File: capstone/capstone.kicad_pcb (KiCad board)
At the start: 2 copper layers, 137.8 x 125.7 mm, 16 parts, among them J1 Conn_01x02, M1 Motor_Servo, M2 Motor_Servo, M3 Stepper_Motor_bipolar, M4 Stepper_Motor_bipolar, SW1 SW_Push, U1 PicoW

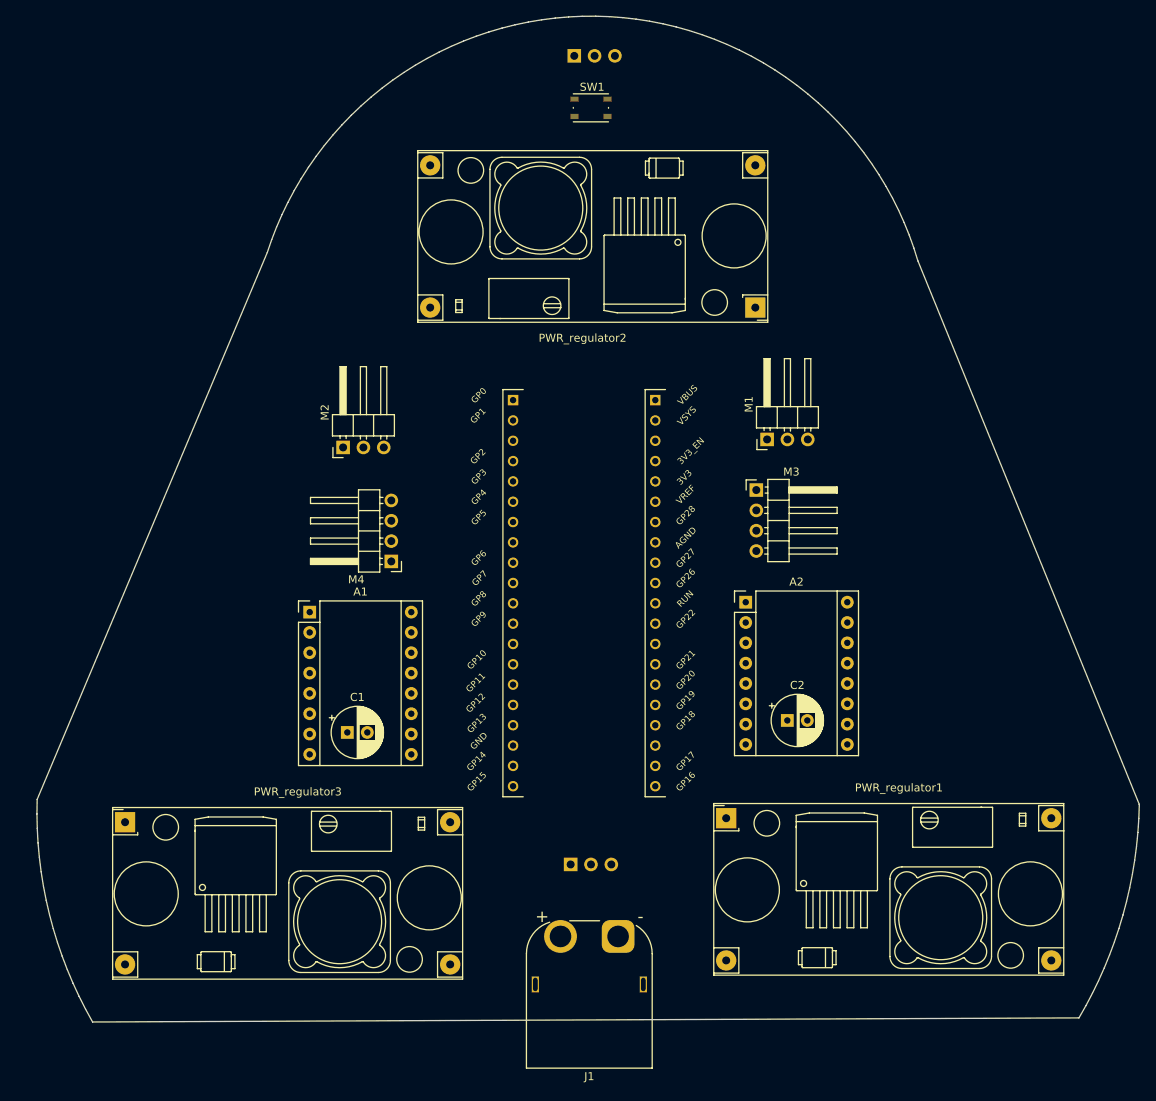
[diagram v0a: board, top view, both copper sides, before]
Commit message: remove 12v regulators + pcb traces
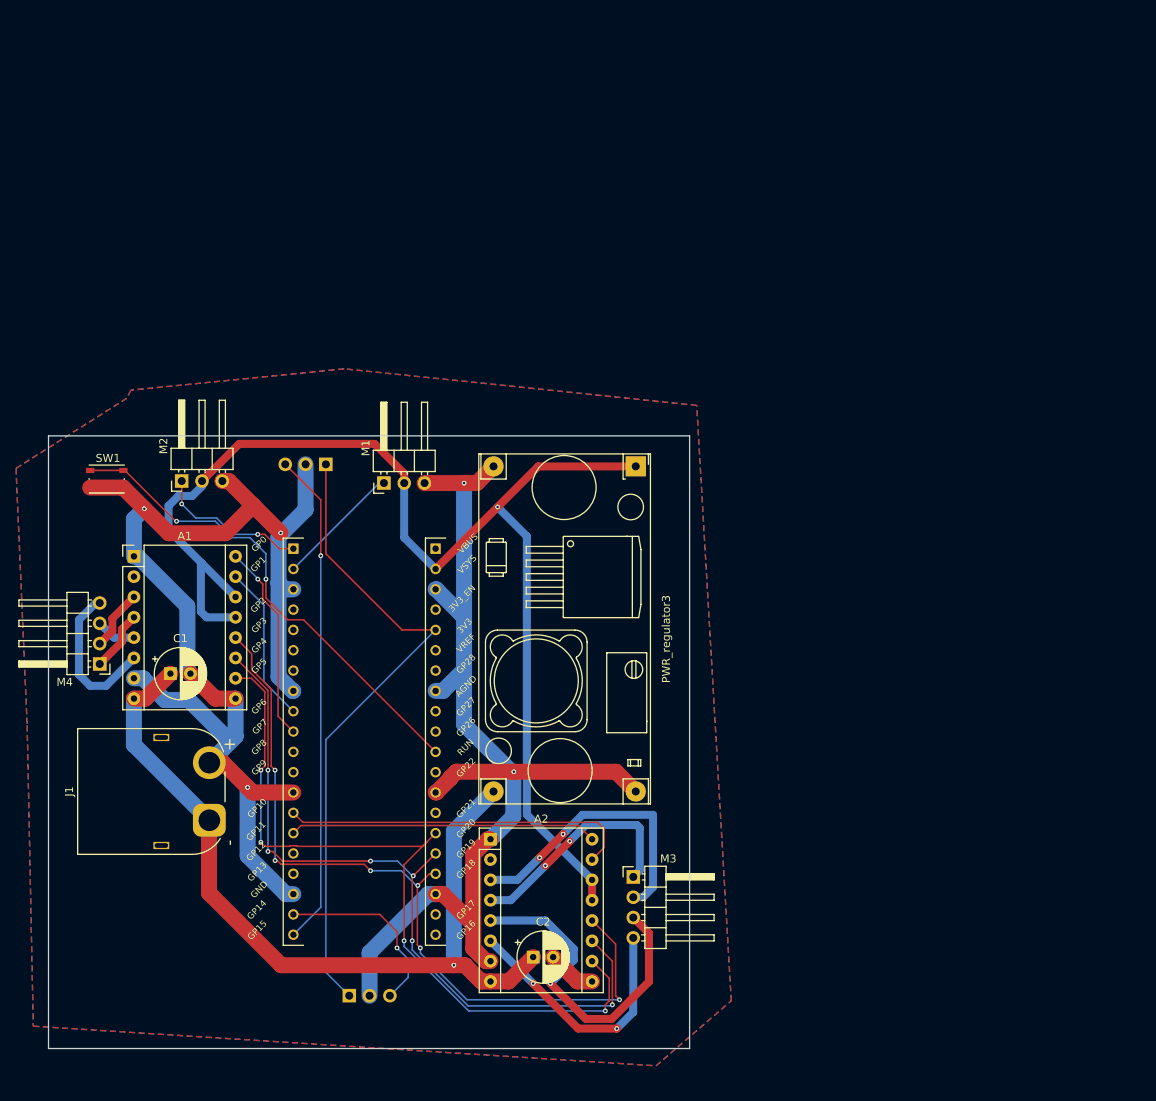
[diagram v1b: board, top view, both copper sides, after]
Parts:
- removed PWR_regulator1, PWR_regulator2: ~, capstone:YAAJ_DCDC_StepDown_LM2596
- moved PWR_regulator3 77.8 mm to (130.6, 88.5), turned to -90 degrees
- moved SW1 76.3 mm to (64.4, 90.1)
- moved IR_sensor2 59.8 mm to (91.8, 88.3), turned to 90 degrees
- moved J1 53.1 mm to (77.3, 132.8), turned to 90 degrees
- moved M3 50.7 mm to (130.2, 139.8)
- moved M1 48.2 mm to (99.1, 90.6)
- moved A2 43.5 mm to (112.4, 135.1)
- moved C2 43.4 mm to (117.7, 149.9)
- moved M4 38.6 mm to (63.6, 113.2)
- moved U1 33.1 mm to (96.5, 120.5)
- moved IR_sensor1 32.2 mm to (94.7, 154.7)
- moved C1 23.3 mm to (72.4, 114.4)
- moved A1 23.1 mm to (67.8, 99.8)
- moved M2 20.6 mm to (73.8, 90.4)
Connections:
- A1 pad 8: Stepper_PWR_12V -> 14V
- A2 pad 8: Stepper_PWR_12V -> 14V
- C1 pad 1: Stepper_PWR_12V -> 14V
- C2 pad 1: Stepper_PWR_12V -> 14V
- J1 pad 1: Lipo -> 14V
- M1 pad 2: /Servo_PWR_5V -> /PICO_PWR_5V
- M2 pad 2: /Servo_PWR_5V -> /PICO_PWR_5V
- PWR_regulator3 pad 3: Lipo -> 14V
- U1 pad 40: VBUS -> unconnected-(U1-VBUS-Pad40)
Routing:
- net GND: track 0.00 -> 292.1 mm, vias 0 -> 5
- net /PICO_PWR_5V: track 0.00 -> 158.1 mm, vias 0 -> 1
- net 14V: track 0.00 -> 104.2 mm, vias 0 -> 1
- net /mode_bit_3: track 0.00 -> 99.2 mm, vias 0 -> 6
- net /mode_bit_1: track 0.00 -> 96.4 mm, vias 0 -> 4
- net /mode_bit_2: track 0.00 -> 95.5 mm, vias 0 -> 6
- net +3V3: track 0.00 -> 81.4 mm
- net /GPIO15: track 0.00 -> 62.1 mm, vias 0 -> 1
- net /RUN: track 0.00 -> 61.1 mm, vias 0 -> 2
- net /GPIO10: track 0.00 -> 44.1 mm
- net /B1_2: track 0.00 -> 42.3 mm, vias 0 -> 1
- net /GPIO11: track 0.00 -> 38.4 mm
- net /A2_2: track 0.00 -> 35.7 mm, vias 0 -> 2
- net /B2_2: track 0.00 -> 32.5 mm, vias 0 -> 2
- net /A1_2: track 0.00 -> 29.2 mm, vias 0 -> 2
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- added copper zone on B.Cu, net GND
- added copper zone on F.Cu, net GND
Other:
- board size 137.8 x 125.7 mm -> 80.1 x 76.6 mm

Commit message: final pcb
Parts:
- added G***: LOGO, LOGO, F.Cu at (62.1, 142.5)
- moved IR_sensor1 2.82 mm to (94.4, 157.5)
- moved SW1 2.76 mm to (63.4, 92.7), turned to 180 degrees
- moved IR_sensor2 2.16 mm to (91.7, 90.4)
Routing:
- net GND: track 292.1 -> 0.00 mm, vias 5 -> 0
- net /B1_1: track 5.01 -> 37.9 mm
- net /mode_bit_3: track 99.2 -> 75.1 mm, vias 6 -> 2
- net /mode_bit_2: track 95.5 -> 75.3 mm, vias 6 -> 0
- net /mode_bit_1: track 96.4 -> 85.5 mm, vias 4 -> 1
- net /GPIO15: track 62.1 -> 60.0 mm
- net /GPIO14: track 23.4 -> 25.2 mm
- net /PICO_PWR_5V: track 158.1 -> 156.8 mm
- net /B2_1: track 19.2 -> 20.2 mm
- net 14V: track 104.2 -> 105.0 mm
- net /RUN: track 61.1 -> 60.4 mm
- net +3V3: track 81.4 -> 82.0 mm
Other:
- board size 80.1 x 76.6 mm -> 77.9 x 74.8 mm
- board text added: "Coder"
- board text added: "Kitty"
- board text added: "by: - Yassine Moumine - Erika Hanner - Katarina Spasic - Kavin Gnanapandithan - Ayman Naciri - Sam Charbonneau"

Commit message: text design
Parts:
- moved G*** 1.78 mm to (62.1, 144.3)
